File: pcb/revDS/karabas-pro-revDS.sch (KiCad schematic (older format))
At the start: 209 parts, among them CON1 CF-CARD, CON2 SD, CON3 VGA, CON4 Joystick, CON5 Keyboard, CON6 Mouse, CON7 Audio, CON8 12V, CON9 MicroSD', J1 Floppy, J10 Ext Joystick, J2 FPGA JTAG, J3 Floppy, J4 uBus, J5 AVR JTAG, J6 AVR UART, J7 ESP-BUS, J8 Tape In, J9 Tape Out, Q1 BC856, SW1 SW_Push, SW2 SW_Push, SW4 SW_SPST, U1 EP4CE6E22C8N, U10 ESP-12E, U11 TDA1543, U12 AMS1117-3.3, U13 AMS1117-2.5, U14 AMS1117-1.2, U15 LM2596S-5, U16 LM311, U17 74LS06, U18 74LS38, U2 CY62167EV30, U3 W25Q16, U3''1 W25Q16, U4 EPM3128ATC100-5, U5 ATMEGA328-AU, U6 MB8877A, U7 TXB0104PW, U8 TXB0104PW, U9 DS1307Z+, X1 SG-7050CAN, Y1 32768Hz, Y2 16MHz

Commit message: Updated pcb rev.DS
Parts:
- U1: value EP4CE6E22C8N -> EP4CE10E22C8N
- U2: value CY62167EV30 -> CY62167EV30LL
- U4: value EPM3128ATC100-5 -> EPM3128ATC100-10N
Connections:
- net L4: now reaches D4.1 (K), R54.2
- net L5: now reaches D6.1 (K), R55.2
- net L3: now reaches D7.2 (A), R56.2
- net L1: now reaches D1.2 (A), R28.2
- net L2: now reaches D2.2 (A), R29.2
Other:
- moved on the sheet: D1, D2, D4, D6, D7
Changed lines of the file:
@@
 P 3550 3300
 F 0 "U1" H 3550 3350 50  0000 L CNN
-F 1 "EP4CE6E22C8N" H 3300 3200 50  0000 L CNN
+F 1 "EP4CE10E22C8N" H 3300 3200 50  0000 L CNN
 F 2 "footprints:ALTERA-QFP-145" H 3550 3300 50  0001 C CNN
 F 3 "" H 3550 3300 50  0001 C CNN
@@
 P 7650 2850
 F 0 "U2" H 7650 4367 50  0000 C CNN
-F 1 "CY62167EV30" H 7650 4276 50  0000 C CNN
+F 1 "CY62167EV30LL" H 7650 4276 50  0000 C CNN
 F 2 "Package_SO:TSOP-I-48_18.4x12mm_P0.5mm" H 7850 4250 50  0001 C CNN
 F 3 "" H 7850 4250 50  0001 C CNN
@@
 P 17400 7750
 F 0 "U4" H 17350 7900 50  0000 L CNN
-F 1 "EPM3128ATC100-5" H 17100 7800 50  0000 L CNN
+F 1 "EPM3128ATC100-10N" H 17100 7800 50  0000 L CNN
 F 2 "Package_QFP:LQFP-100_14x14mm_P0.5mm" H 17400 7750 50  0001 C CNN
 F 3 "" H 17400 7750 50  0001 C CNN
@@
 L Device:LED D1
 U 1 1 63476C53
-P 15000 1050
-F 0 "D1" H 14993 1267 50  0000 C CNN
-F 1 "KBD" H 14993 1176 50  0000 C CNN
-F 2 "LED_SMD:LED_0805_2012Metric_Pad1.15x1.40mm_HandSolder" H 15000 1050 50  0001 C CNN
-F 3 "~" H 15000 1050 50  0001 C CNN
-	1    15000 1050
+P 15450 1050
+F 0 "D1" H 15443 1267 50  0000 C CNN
+F 1 "KBD" H 15443 1176 50  0000 C CNN
+F 2 "LED_SMD:LED_0805_2012Metric_Pad1.15x1.40mm_HandSolder" H 15450 1050 50  0001 C CNN
+F 3 "~" H 15450 1050 50  0001 C CNN
+	1    15450 1050
 	-1   0    0    -1
 $EndComp
@@
 L Device:LED D2
 U 1 1 6358E103
-P 15000 1400
-F 0 "D2" H 14993 1617 50  0000 C CNN
-F 1 "ACT" H 14993 1526 50  0000 C CNN
-F 2 "LED_SMD:LED_0805_2012Metric_Pad1.15x1.40mm_HandSolder" H 15000 1400 50  0001 C CNN
-F 3 "~" H 15000 1400 50  0001 C CNN
-	1    15000 1400
+P 15450 1400
+F 0 "D2" H 15443 1617 50  0000 C CNN
+F 1 "ACT" H 15443 1526 50  0000 C CNN
+F 2 "LED_SMD:LED_0805_2012Metric_Pad1.15x1.40mm_HandSolder" H 15450 1400 50  0001 C CNN
+F 3 "~" H 15450 1400 50  0001 C CNN
+	1    15450 1400
 	-1   0    0    -1
 $EndComp
@@
 L power:GND #PWR0153
 U 1 1 63619442
-P 15300 1850
-F 0 "#PWR0153" H 15300 1600 50  0001 C CNN
-F 1 "GND" H 15305 1677 50  0000 C CNN
-F 2 "" H 15300 1850 50  0001 C CNN
-F 3 "" H 15300 1850 50  0001 C CNN
-	1    15300 1850
+P 15750 1850
+F 0 "#PWR0153" H 15750 1600 50  0001 C CNN
+F 1 "GND" H 15755 1677 50  0000 C CNN
+F 2 "" H 15750 1850 50  0001 C CNN
+F 3 "" H 15750 1850 50  0001 C CNN
+	1    15750 1850
 	1    0    0    -1
 $EndComp
 Wire Wire Line
-	15150 1050 15300 1050
+	15600 1050 15750 1050
 Wire Wire Line
-	15300 1050 15300 1400
+	15750 1050 15750 1400
 Wire Wire Line
-	15150 1400 15300 1400
-Connection ~ 15300 1400
+	15600 1400 15750 1400
+Connection ~ 15750 1400
 $Comp
 L power:GND #PWR0154
@@
 L Device:LED D4
 U 1 1 623E5E10
-P 15550 2650
-F 0 "D4" H 15543 2867 50  0000 C CNN
-F 1 "SD" H 15543 2776 50  0000 C CNN
-F 2 "LED_SMD:LED_0805_2012Metric_Pad1.15x1.40mm_HandSolder" H 15550 2650 50  0001 C CNN
-F 3 "~" H 15550 2650 50  0001 C CNN
-	1    15550 2650
+P 15650 2650
+F 0 "D4" H 15643 2867 50  0000 C CNN
+F 1 "SD" H 15643 2776 50  0000 C CNN
+F 2 "LED_SMD:LED_0805_2012Metric_Pad1.15x1.40mm_HandSolder" H 15650 2650 50  0001 C CNN
+F 3 "~" H 15650 2650 50  0001 C CNN
+	1    15650 2650
 	1    0    0    -1
 $EndComp
@@
 L Device:LED D6
 U 1 1 624DC115
-P 15600 3550
-F 0 "D6" H 15593 3767 50  0000 C CNN
-F 1 "CF" H 15593 3676 50  0000 C CNN
-F 2 "LED_SMD:LED_0805_2012Metric_Pad1.15x1.40mm_HandSolder" H 15600 3550 50  0001 C CNN
-F 3 "~" H 15600 3550 50  0001 C CNN
-	1    15600 3550
+P 15700 3550
+F 0 "D6" H 15693 3767 50  0000 C CNN
+F 1 "CF" H 15693 3676 50  0000 C CNN
+F 2 "LED_SMD:LED_0805_2012Metric_Pad1.15x1.40mm_HandSolder" H 15700 3550 50  0001 C CNN
+F 3 "~" H 15700 3550 50  0001 C CNN
+	1    15700 3550
 	1    0    0    -1
 $EndComp
@@
 L Device:LED D7
 U 1 1 624DCCE8
-P 15000 1750
-F 0 "D7" H 14993 1967 50  0000 C CNN
-F 1 "PWR" H 14993 1876 50  0000 C CNN
-F 2 "LED_SMD:LED_0805_2012Metric_Pad1.15x1.40mm_HandSolder" H 15000 1750 50  0001 C CNN
-F 3 "~" H 15000 1750 50  0001 C CNN
-	1    15000 1750
+P 15450 1750
+F 0 "D7" H 15443 1967 50  0000 C CNN
+F 1 "PWR" H 15443 1876 50  0000 C CNN
+F 2 "LED_SMD:LED_0805_2012Metric_Pad1.15x1.40mm_HandSolder" H 15450 1750 50  0001 C CNN
+F 3 "~" H 15450 1750 50  0001 C CNN
+	1    15450 1750
 	-1   0    0    -1
 $EndComp
 Wire Wire Line
-	15150 1750 15300 1750
+	15600 1750 15750 1750
 Entry Wire Line
 	14200 1650 14300 1750
@@
 L vcc33:VCC3_3 #PWR0198
 U 1 1 637CD61A
-P 15750 2500
-F 0 "#PWR0198" H 15750 2350 50  0001 C CNN
-F 1 "VCC3_3" H 15700 2650 50  0000 C CNN
-F 2 "" H 15750 2500 50  0001 C CNN
-F 3 "" H 15750 2500 50  0001 C CNN
-	1    15750 2500
+P 15850 2500
+F 0 "#PWR0198" H 15850 2350 50  0001 C CNN
+F 1 "VCC3_3" H 15800 2650 50  0000 C CNN
+F 2 "" H 15850 2500 50  0001 C CNN
+F 3 "" H 15850 2500 50  0001 C CNN
+	1    15850 2500
 	1    0    0    -1
 $EndComp
 Wire Wire Line
-	15750 2500 15750 2650
+	15850 2500 15850 2650
 Wire Wire Line
-	15750 2650 15700 2650
-Connection ~ 15750 2650
+	15850 2650 15800 2650
+Connection ~ 15850 2650
 Wire Wire Line
 	14900 2650 15000 2650
 Wire Wire Line
-	15300 2650 15400 2650
+	15300 2650 15500 2650
 Wire Wire Line
-	15300 3550 15450 3550
+	15300 3550 15550 3550
 Wire Wire Line
-	15300 1400 15300 1750
-Connection ~ 15300 1750
+	15750 1400 15750 1750
+Connection ~ 15750 1750
 Wire Wire Line
-	15300 1750 15300 1850
+	15750 1750 15750 1850
 $Comp
 L vcc33:VCC3_3 #PWR0199
@@
 	14300 3550 15000 3550
 Wire Wire Line
-	15750 2650 15750 3550
+	15850 2650 15850 3550
 Text Label 14300 3550 0    50   ~ 0
 LED_BUSY
@@
 Text Label 12350 5450 2    50   ~ 0
 JOY_R2
+Wire Wire Line
+	14850 1050 15300 1050
+Wire Wire Line
+	14850 1400 15300 1400
+Wire Wire Line
+	14850 1750 15300 1750
+Text Label 15250 1050 2    50   ~ 0
+L1
+Text Label 15250 1400 2    50   ~ 0
+L2
+Text Label 15250 1750 2    50   ~ 0
+L3
+Text Label 15450 2650 2    50   ~ 0
+L4
+Text Label 15450 3550 2    50   ~ 0
+L5
 Wire Bus Line
 	4850 6350 5350 6350

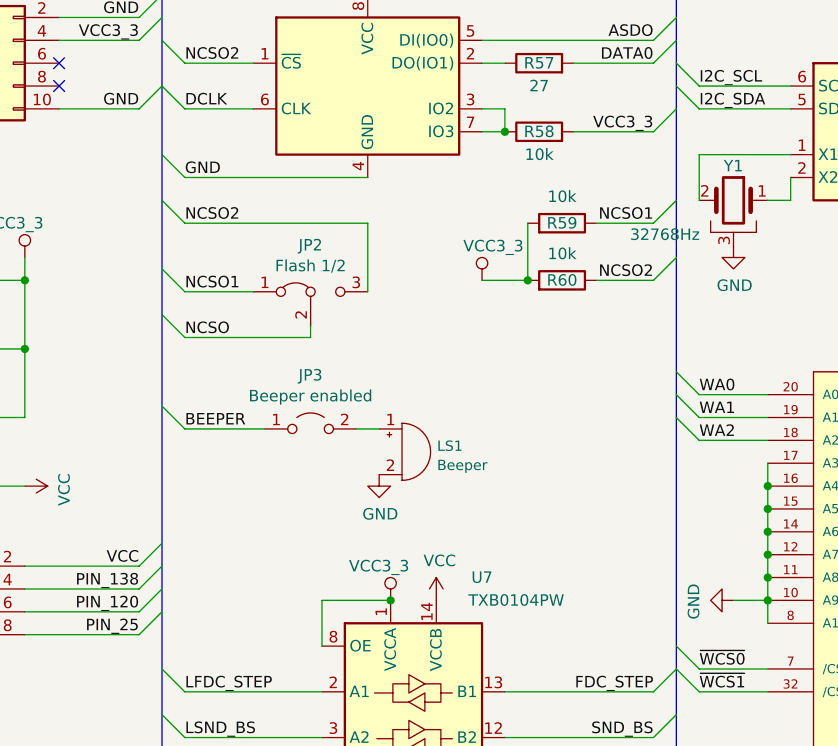
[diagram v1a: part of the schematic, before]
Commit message: updated revDS: added diode and transistor before buzzer
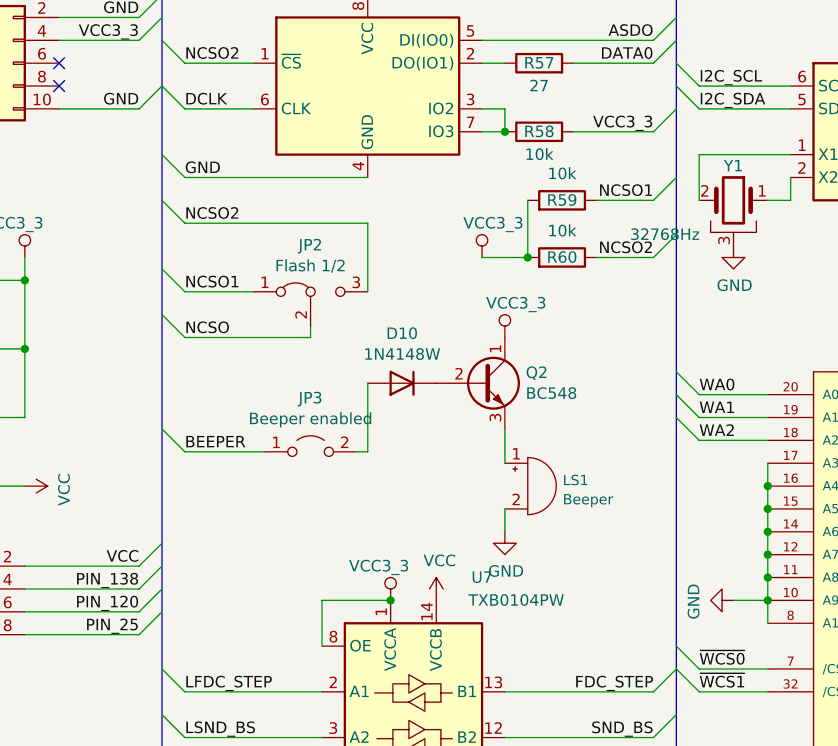
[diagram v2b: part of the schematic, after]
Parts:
- added D10: 1N4148W, Diode_SMD:D_SOD-123, symbol Diode:1N4148W
- added Q2: BC548, Package_TO_SOT_SMD:SOT-23, symbol Transistor_BJT:BC548
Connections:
- net VCC3_3: now also Q2.1 (C)
- net at LS1.1 (-): now also Q2.3 (E); no longer JP3.2 (B)
- new net: D10.1 (K), Q2.2 (B)
- new net: D10.2 (A), JP3.2 (B)
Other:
- moved on the sheet: JP3, LS1, R59, R60
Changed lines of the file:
@@
 L Device:R R60
 U 1 1 606E6EEB
-P 8250 8250
-F 0 "R60" V 8250 8250 50  0000 C CNN
-F 1 "10k" V 8366 8250 50  0000 C CNN
-F 2 "Resistor_SMD:R_0805_2012Metric_Pad1.15x1.40mm_HandSolder" V 8180 8250 50  0001 C CNN
-F 3 "~" H 8250 8250 50  0001 C CNN
-	1    8250 8250
+P 8250 8150
+F 0 "R60" V 8250 8150 50  0000 C CNN
+F 1 "10k" V 8366 8150 50  0000 C CNN
+F 2 "Resistor_SMD:R_0805_2012Metric_Pad1.15x1.40mm_HandSolder" V 8180 8150 50  0001 C CNN
+F 3 "~" H 8250 8150 50  0001 C CNN
+	1    8250 8150
 	0    1    -1   0
 $EndComp
@@
 L Device:R R59
 U 1 1 606F3688
-P 8250 8000
-F 0 "R59" V 8250 8000 50  0000 C CNN
-F 1 "10k" V 8366 8000 50  0000 C CNN
-F 2 "Resistor_SMD:R_0805_2012Metric_Pad1.15x1.40mm_HandSolder" V 8180 8000 50  0001 C CNN
-F 3 "~" H 8250 8000 50  0001 C CNN
-	1    8250 8000
+P 8250 7900
+F 0 "R59" V 8250 7900 50  0000 C CNN
+F 1 "10k" V 8366 7900 50  0000 C CNN
+F 2 "Resistor_SMD:R_0805_2012Metric_Pad1.15x1.40mm_HandSolder" V 8180 7900 50  0001 C CNN
+F 3 "~" H 8250 7900 50  0001 C CNN
+	1    8250 7900
 	0    1    -1   0
 $EndComp
 Entry Wire Line
-	8750 7900 8650 8000
-Entry Wire Line
-	8750 8150 8650 8250
-Wire Wire Line
-	8650 8000 8400 8000
-Wire Wire Line
-	8650 8250 8400 8250
+	8750 7800 8650 7900
+Entry Wire Line
+	8750 8050 8650 8150
+Wire Wire Line
+	8650 7900 8400 7900
+Wire Wire Line
+	8650 8150 8400 8150
 $Comp
 L vcc33:VCC3_3 #PWR03
 U 1 1 608FE7F4
-P 7900 8250
-F 0 "#PWR03" H 7900 8100 50  0001 C CNN
-F 1 "VCC3_3" H 7850 8400 50  0000 C CNN
-F 2 "" H 7900 8250 50  0001 C CNN
-F 3 "" H 7900 8250 50  0001 C CNN
-	1    7900 8250
+P 7900 8150
+F 0 "#PWR03" H 7900 8000 50  0001 C CNN
+F 1 "VCC3_3" H 7850 8300 50  0000 C CNN
+F 2 "" H 7900 8150 50  0001 C CNN
+F 3 "" H 7900 8150 50  0001 C CNN
+	1    7900 8150
 	-1   0    0    -1
 $EndComp
 Wire Wire Line
-	8100 8000 8100 8250
-Connection ~ 8100 8250
-Wire Wire Line
-	8100 8250 7900 8250
-Text Label 8650 8000 2    50   ~ 0
+	8100 7900 8100 8150
+Connection ~ 8100 8150
+Wire Wire Line
+	8100 8150 7900 8150
+Text Label 8650 7900 2    50   ~ 0
 NCSO1
-Text Label 8650 8250 2    50   ~ 0
+Text Label 8650 8150 2    50   ~ 0
 NCSO2
 $Comp
@@
 L Device:Buzzer LS1
 U 1 1 63A63093
-P 7550 9000
-F 0 "LS1" H 7703 9025 45  0000 L CNN
-F 1 "Beeper" H 7703 8941 45  0000 L CNN
-F 2 "Buzzer_Beeper:Buzzer_12x9.5RM7.6" H 7550 9300 20  0001 C CNN
-F 3 "" H 7550 9000 50  0001 C CNN
-F 4 "COMP-08253" H 7703 8899 60  0001 L CNN "Field4"
-	1    7550 9000
-	1    0    0    -1
-$EndComp
-Entry Wire Line
-	6500 8800 6600 8900
+P 8100 9150
+F 0 "LS1" H 8253 9175 45  0000 L CNN
+F 1 "Beeper" H 8253 9091 45  0000 L CNN
+F 2 "Buzzer_Beeper:Buzzer_12x9.5RM7.6" H 8100 9450 20  0001 C CNN
+F 3 "" H 8100 9150 50  0001 C CNN
+F 4 "COMP-08253" H 8253 9049 60  0001 L CNN "Field4"
+	1    8100 9150
+	1    0    0    -1
+$EndComp
+Entry Wire Line
+	6500 8900 6600 9000
 $Comp
 L power:GND #PWR0213
 U 1 1 63D1AB83
-P 7450 9100
-F 0 "#PWR0213" H 7450 8850 50  0001 C CNN
-F 1 "GND" H 7455 8927 50  0000 C CNN
-F 2 "" H 7450 9100 50  0001 C CNN
-F 3 "" H 7450 9100 50  0001 C CNN
-	1    7450 9100
+P 8000 9350
+F 0 "#PWR0213" H 8000 9100 50  0001 C CNN
+F 1 "GND" H 8005 9177 50  0000 C CNN
+F 2 "" H 8000 9350 50  0001 C CNN
+F 3 "" H 8000 9350 50  0001 C CNN
+	1    8000 9350
 	1    0    0    -1
 $EndComp
@@
 L Jumper:Jumper_2_Open JP3
 U 1 1 643BF174
-P 7150 8900
-F 0 "JP3" H 7150 9135 50  0000 C CNN
-F 1 "Beeper enabled" H 7150 9044 50  0000 C CNN
-F 2 "Connector_PinHeader_2.54mm:PinHeader_1x02_P2.54mm_Vertical" H 7150 8900 50  0001 C CNN
-F 3 "~" H 7150 8900 50  0001 C CNN
-	1    7150 8900
-	1    0    0    -1
-$EndComp
-Wire Wire Line
-	6600 8900 6950 8900
-Wire Wire Line
-	7350 8900 7450 8900
-Text Label 6600 8900 0    50   ~ 0
+P 7150 9000
+F 0 "JP3" H 7150 9235 50  0000 C CNN
+F 1 "Beeper enabled" H 7150 9144 50  0000 C CNN
+F 2 "Connector_PinHeader_2.54mm:PinHeader_1x02_P2.54mm_Vertical" H 7150 9000 50  0001 C CNN
+F 3 "~" H 7150 9000 50  0001 C CNN
+	1    7150 9000
+	1    0    0    -1
+$EndComp
+Wire Wire Line
+	6600 9000 6950 9000
+Text Label 6600 9000 0    50   ~ 0
 BEEPER
 Entry Wire Line
@@
 Text Label 15450 3550 2    50   ~ 0
 L5
+$Comp
+L Transistor_BJT:BC548 Q2
+U 1 1 60A22677
+P 7900 8700
+F 0 "Q2" H 8091 8746 50  0000 L CNN
+F 1 "BC548" H 8091 8655 50  0000 L CNN
+F 2 "Package_TO_SOT_SMD:SOT-23" H 8100 8625 50  0001 L CIN
+F 3 "https://www.onsemi.com/pub/Collateral/BC550-D.pdf" H 7900 8700 50  0001 L CNN
+	1    7900 8700
+	1    0    0    -1
+$EndComp
+$Comp
+L vcc33:VCC3_3 #PWR0180
+U 1 1 60B9C5F6
+P 8000 8500
+F 0 "#PWR0180" H 8000 8350 50  0001 C CNN
+F 1 "VCC3_3" H 7950 8650 50  0000 C CNN
+F 2 "" H 8000 8500 50  0001 C CNN
+F 3 "" H 8000 8500 50  0001 C CNN
+	1    8000 8500
+	-1   0    0    -1
+$EndComp
+$Comp
+L Diode:1N4148W D10
+U 1 1 610F16F8
+P 7550 8700
+F 0 "D10" H 7550 8483 50  0000 C CNN
+F 1 "1N4148W" H 7550 8574 50  0000 C CNN
+F 2 "Diode_SMD:D_SOD-123" H 7550 8525 50  0001 C CNN
+F 3 "https://www.vishay.com/docs/85748/1n4148w.pdf" H 7550 8700 50  0001 C CNN
+	1    7550 8700
+	-1   0    0    1
+$EndComp
+Wire Wire Line
+	8000 9350 8000 9250
+Wire Wire Line
+	8000 9050 8000 8900
+Wire Wire Line
+	7350 9000 7400 9000
+Wire Wire Line
+	7400 9000 7400 8700
 Wire Bus Line
 	4850 6350 5350 6350

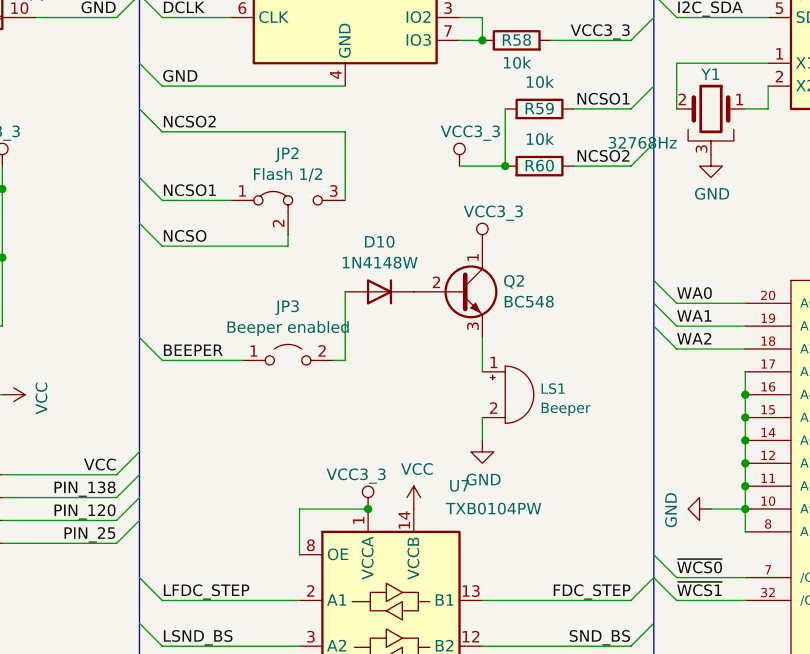
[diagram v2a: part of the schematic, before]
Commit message: Added missing R for buzzer
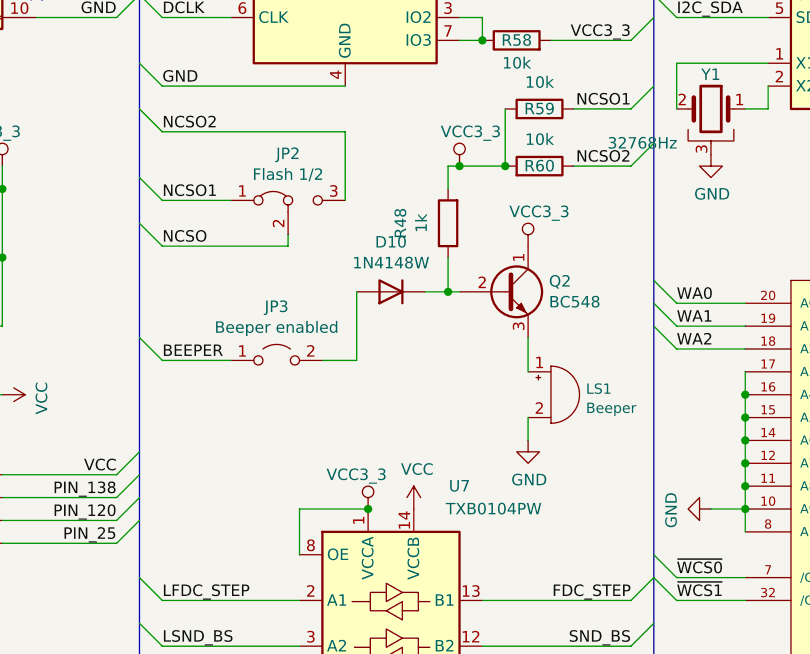
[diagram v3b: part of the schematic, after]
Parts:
- added R48: 1k, Resistor_SMD:R_0805_2012Metric_Pad1.20x1.40mm_HandSolder, symbol Device:R
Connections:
- net VCC3_3: now also R48.2
- net at D10.1 (K), Q2.2 (B): now also R48.1
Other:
- moved on the sheet: D10, JP3, LS1, Q2
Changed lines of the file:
@@
 L Device:Buzzer LS1
 U 1 1 63A63093
-P 8100 9150
-F 0 "LS1" H 8253 9175 45  0000 L CNN
-F 1 "Beeper" H 8253 9091 45  0000 L CNN
-F 2 "Buzzer_Beeper:Buzzer_12x9.5RM7.6" H 8100 9450 20  0001 C CNN
-F 3 "" H 8100 9150 50  0001 C CNN
-F 4 "COMP-08253" H 8253 9049 60  0001 L CNN "Field4"
-	1    8100 9150
+P 8300 9150
+F 0 "LS1" H 8453 9175 45  0000 L CNN
+F 1 "Beeper" H 8453 9091 45  0000 L CNN
+F 2 "Buzzer_Beeper:Buzzer_12x9.5RM7.6" H 8300 9450 20  0001 C CNN
+F 3 "" H 8300 9150 50  0001 C CNN
+F 4 "COMP-08253" H 8453 9049 60  0001 L CNN "Field4"
+	1    8300 9150
 	1    0    0    -1
 $EndComp
@@
 L power:GND #PWR0213
 U 1 1 63D1AB83
-P 8000 9350
-F 0 "#PWR0213" H 8000 9100 50  0001 C CNN
-F 1 "GND" H 8005 9177 50  0000 C CNN
-F 2 "" H 8000 9350 50  0001 C CNN
-F 3 "" H 8000 9350 50  0001 C CNN
-	1    8000 9350
+P 8200 9350
+F 0 "#PWR0213" H 8200 9100 50  0001 C CNN
+F 1 "GND" H 8205 9177 50  0000 C CNN
+F 2 "" H 8200 9350 50  0001 C CNN
+F 3 "" H 8200 9350 50  0001 C CNN
+	1    8200 9350
 	1    0    0    -1
 $EndComp
@@
 L Jumper:Jumper_2_Open JP3
 U 1 1 643BF174
-P 7150 9000
-F 0 "JP3" H 7150 9235 50  0000 C CNN
-F 1 "Beeper enabled" H 7150 9144 50  0000 C CNN
-F 2 "Connector_PinHeader_2.54mm:PinHeader_1x02_P2.54mm_Vertical" H 7150 9000 50  0001 C CNN
-F 3 "~" H 7150 9000 50  0001 C CNN
-	1    7150 9000
-	1    0    0    -1
-$EndComp
-Wire Wire Line
-	6600 9000 6950 9000
+P 7100 9000
+F 0 "JP3" H 7100 9235 50  0000 C CNN
+F 1 "Beeper enabled" H 7100 9144 50  0000 C CNN
+F 2 "Connector_PinHeader_2.54mm:PinHeader_1x02_P2.54mm_Vertical" H 7100 9000 50  0001 C CNN
+F 3 "~" H 7100 9000 50  0001 C CNN
+	1    7100 9000
+	1    0    0    -1
+$EndComp
+Wire Wire Line
+	6600 9000 6900 9000
 Text Label 6600 9000 0    50   ~ 0
 BEEPER
@@
 L Transistor_BJT:BC548 Q2
 U 1 1 60A22677
-P 7900 8700
-F 0 "Q2" H 8091 8746 50  0000 L CNN
-F 1 "BC548" H 8091 8655 50  0000 L CNN
-F 2 "Package_TO_SOT_SMD:SOT-23" H 8100 8625 50  0001 L CIN
-F 3 "https://www.onsemi.com/pub/Collateral/BC550-D.pdf" H 7900 8700 50  0001 L CNN
-	1    7900 8700
+P 8100 8700
+F 0 "Q2" H 8291 8746 50  0000 L CNN
+F 1 "BC548" H 8291 8655 50  0000 L CNN
+F 2 "Package_TO_SOT_SMD:SOT-23" H 8300 8625 50  0001 L CIN
+F 3 "https://www.onsemi.com/pub/Collateral/BC550-D.pdf" H 8100 8700 50  0001 L CNN
+	1    8100 8700
 	1    0    0    -1
 $EndComp
@@
 L vcc33:VCC3_3 #PWR0180
 U 1 1 60B9C5F6
-P 8000 8500
-F 0 "#PWR0180" H 8000 8350 50  0001 C CNN
-F 1 "VCC3_3" H 7950 8650 50  0000 C CNN
-F 2 "" H 8000 8500 50  0001 C CNN
-F 3 "" H 8000 8500 50  0001 C CNN
-	1    8000 8500
+P 8200 8500
+F 0 "#PWR0180" H 8200 8350 50  0001 C CNN
+F 1 "VCC3_3" H 8150 8650 50  0000 C CNN
+F 2 "" H 8200 8500 50  0001 C CNN
+F 3 "" H 8200 8500 50  0001 C CNN
+	1    8200 8500
 	-1   0    0    -1
 $EndComp
@@
 L Diode:1N4148W D10
 U 1 1 610F16F8
-P 7550 8700
-F 0 "D10" H 7550 8483 50  0000 C CNN
-F 1 "1N4148W" H 7550 8574 50  0000 C CNN
-F 2 "Diode_SMD:D_SOD-123" H 7550 8525 50  0001 C CNN
-F 3 "https://www.vishay.com/docs/85748/1n4148w.pdf" H 7550 8700 50  0001 C CNN
-	1    7550 8700
+P 7600 8700
+F 0 "D10" H 7600 8483 50  0000 C CNN
+F 1 "1N4148W" H 7600 8574 50  0000 C CNN
+F 2 "Diode_SMD:D_SOD-123" H 7600 8525 50  0001 C CNN
+F 3 "https://www.vishay.com/docs/85748/1n4148w.pdf" H 7600 8700 50  0001 C CNN
+	1    7600 8700
 	-1   0    0    1
 $EndComp
 Wire Wire Line
-	8000 9350 8000 9250
-Wire Wire Line
-	8000 9050 8000 8900
-Wire Wire Line
-	7350 9000 7400 9000
-Wire Wire Line
-	7400 9000 7400 8700
+	8200 9350 8200 9250
+Wire Wire Line
+	8200 9050 8200 8900
+Wire Wire Line
+	7300 9000 7450 9000
+Wire Wire Line
+	7450 9000 7450 8700
+$Comp
+L Device:R R48
+U 1 1 608D1972
+P 7850 8400
+F 0 "R48" V 8057 8400 50  0000 C CNN
+F 1 "1k" V 7966 8400 50  0000 C CNN
+F 2 "Resistor_SMD:R_0805_2012Metric_Pad1.20x1.40mm_HandSolder" V 7780 8400 50  0001 C CNN
+F 3 "~" H 7850 8400 50  0001 C CNN
+	1    7850 8400
+	-1   0    0    1
+$EndComp
+Wire Wire Line
+	7750 8700 7850 8700
+Wire Wire Line
+	7850 8550 7850 8700
+Connection ~ 7850 8700
+Wire Wire Line
+	7850 8700 7900 8700
+Wire Wire Line
+	7850 8250 7850 8150
+Wire Wire Line
+	7850 8150 7900 8150
 Wire Bus Line
 	4850 6350 5350 6350
@@
 Wire Bus Line
 	6500 700  6500 12500
+Connection ~ 7900 8150
 $EndSCHEMATC

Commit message: latest version
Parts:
- added C59, C60, C61, C62: 1uF, Capacitor_SMD:C_0805_2012Metric_Pad1.18x1.45mm_HandSolder, symbol Device:C
- added U19, U20: AMS1117-3.3, Package_TO_SOT_SMD:TO-252-2, symbol Regulator_Linear:AMS1117-3.3
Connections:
- net GND: now also C59.2, C60.2, C61.2, C62.2, U19.1 (GND), U20.1 (GND)
- net VCC: now also C59.1, C61.1, U19.3 (VI), U20.3 (VI)
- net VCC3_3: no longer C13.1, C18.1, C54.1, CON1.13 (VCC2), CON1.38 (VCC1), CON2.4 (VDD), CON9.4 (VDD), D4.2 (A), D6.2 (A), J7.10 (Pin_10), R30.2, R31.2, R36.2, R37.1, R52.2, R74.1, R75.1, U10.8 (VCC)
- new net +3.3ESP: C13.1, C18.1, C54.1, C60.1, J7.10 (Pin_10), R30.2, R31.2, U10.8 (VCC), U19.2 (VO)
- new net +3.3VP: C62.1, CON1.13 (VCC2), CON1.38 (VCC1), CON2.4 (VDD), CON9.4 (VDD), D4.2 (A), D6.2 (A), R36.2, R37.1, R52.2, R74.1, R75.1, U20.2 (VO)
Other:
- moved on the sheet: C13, C18, C54

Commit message: Revert "latest version"
This reverts commit fe14166d25968ab133076a7a9191b22261ce910e.
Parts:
- removed C59, C60, C61, C62: 1uF, Capacitor_SMD:C_0805_2012Metric_Pad1.18x1.45mm_HandSolder, symbol Device:C
- removed U19, U20: AMS1117-3.3, Package_TO_SOT_SMD:TO-252-2, symbol Regulator_Linear:AMS1117-3.3
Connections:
- net +3.3ESP is gone; now on net VCC3_3: C13.1, C18.1, C54.1, J7.10 (Pin_10), R30.2, R31.2, U10.8 (VCC)
- net +3.3VP is gone; now on net VCC3_3: CON1.13 (VCC2), CON1.38 (VCC1), CON2.4 (VDD), CON9.4 (VDD), D4.2 (A), D6.2 (A), R36.2, R37.1, R52.2, R74.1, R75.1
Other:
- moved on the sheet: C13, C18, C54
